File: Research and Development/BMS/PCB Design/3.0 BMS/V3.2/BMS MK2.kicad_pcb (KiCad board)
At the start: 2 copper layers, 174.6 x 98.4 mm, 42 parts, among them J1 JST CONN OUT, J3 JST CONN IN, J4 B+, J7 B-, Q1 AO3400A, Q2 PN100, Q3 AO3407, Q4 AO3407, Q7 PN100, SW1 SW_DPDT_x2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

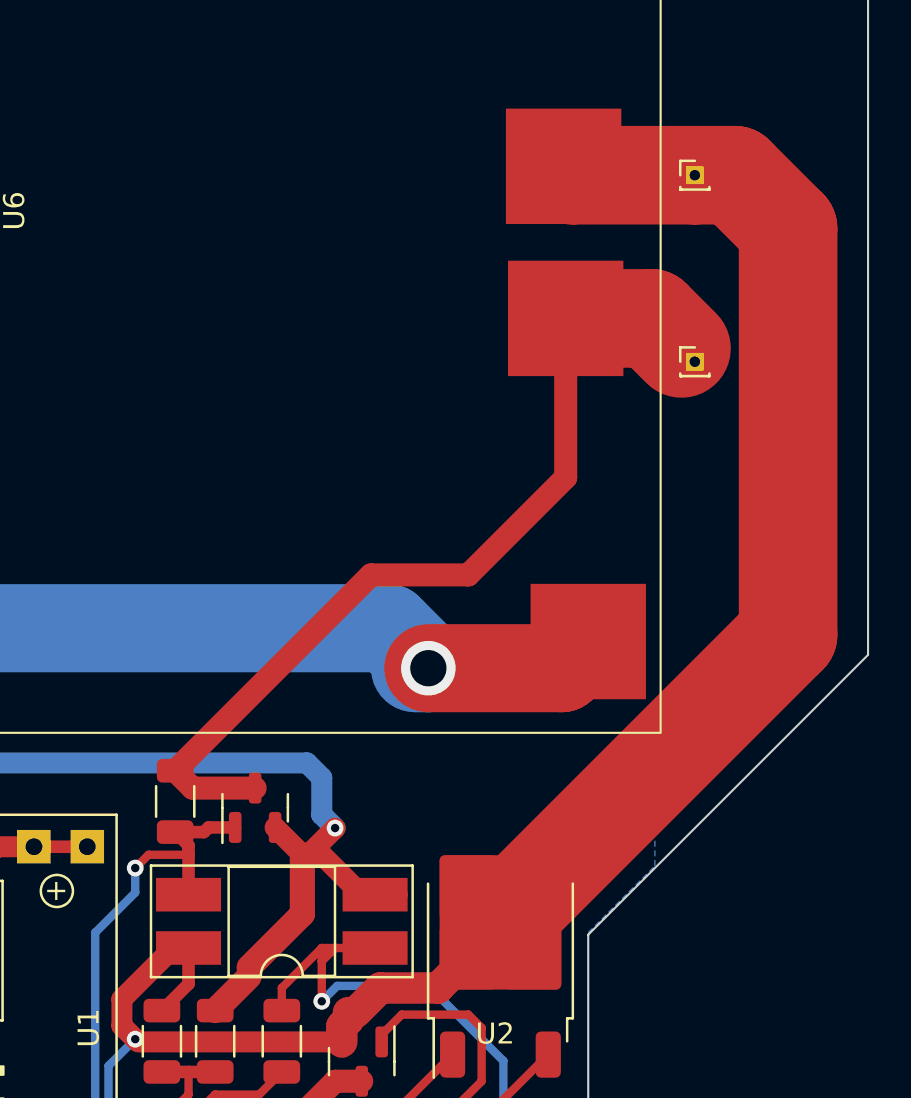
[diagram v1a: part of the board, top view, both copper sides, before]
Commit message: updated PCB and tidied up schematic BMS
Not final version. will revamp the charger in with 5 pins, 1 power for charging and powering load.
so charging section will be re implemented.

more 3d models added to board, bms etc
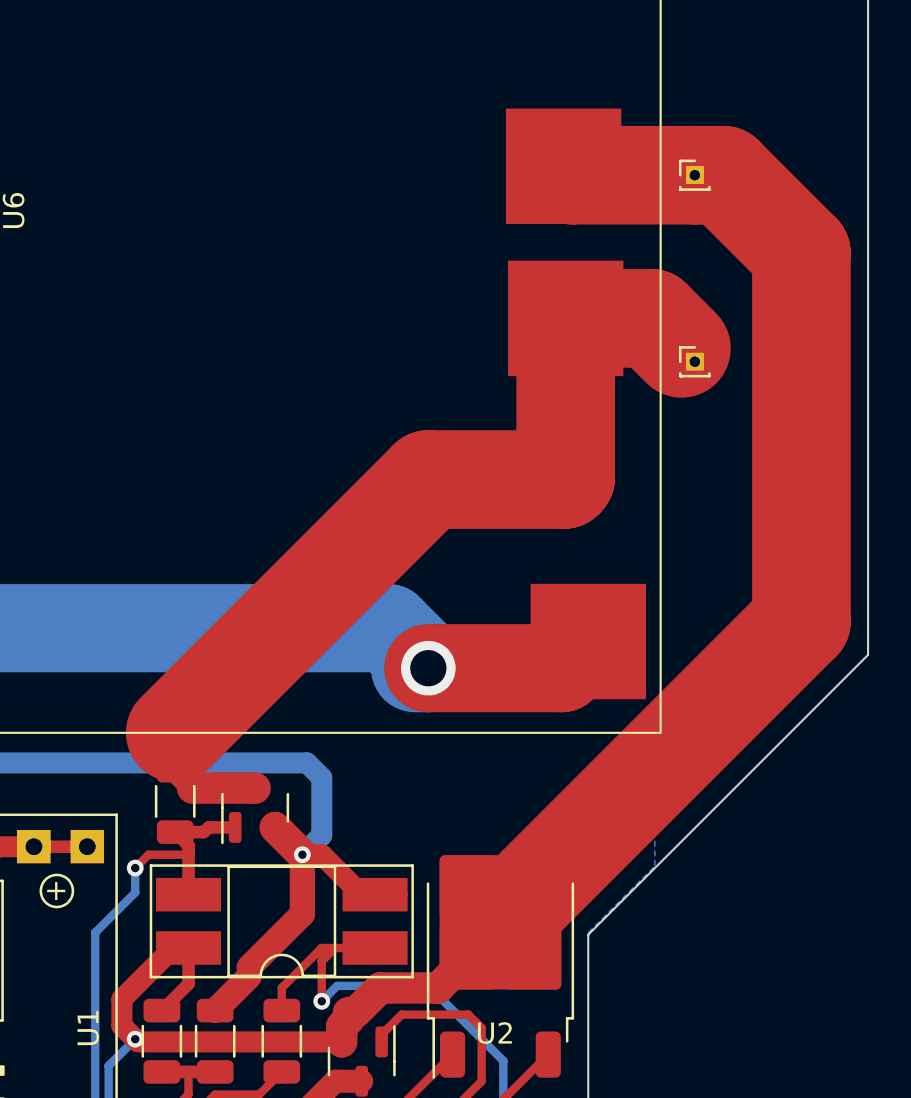
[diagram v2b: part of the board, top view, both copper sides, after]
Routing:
- net Batt -: track 42.5 -> 41.7 mm
- net GND: track 304.4 -> 303.7 mm
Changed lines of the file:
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@@
     (pad "7" smd rect (at 39.825 -3.9 90) (size 5.5 5.5) (layers "F.Cu" "F.Paste" "F.Mask")
       (net 24 "Net-(B4-B1-)") (pinfunction "16.8V") (pintype "input"))
+    (model "C:/Users/acste/Downloads/bms-4s-40a-60a-1.snapshot.2/BMS 4S 40A.STEP"
+      (offset (xyz 45.5 0 0))
+      (scale (xyz 1 1 1))
+      (rotate (xyz 0 0 -90))
+    )
   )
   (footprint "Capacitor_SMD:C_1206_3216Metric" (layer "F.Cu")
@@
   (segment (start 197.32 134.21) (end 195.58 135.95) (width 0.4) (layer "F.Cu") (net 1))
   (segment (start 201.295 115.57) (end 201.295 114.3) (width 1) (layer "F.Cu") (net 1))
+  (segment (start 229.97 75.03) (end 228.6 75.03) (width 4.7) (layer "F.Cu") (net 1))
   (segment (start 203.735 111.86) (end 204.47 111.86) (width 0.4) (layer "F.Cu") (net 1))
   (segment (start 201.295 114.3) (end 203.735 111.86) (width 1) (layer "F.Cu") (net 1))
   (segment (start 212.437501 114.935) (end 213.607501 113.765) (width 1.5) (layer "F.Cu") (net 1))
   (segment (start 204.47 111.86) (end 204.47 113.5725) (width 0.6) (layer "F.Cu") (net 1))
-  (segment (start 233.045 77.57) (end 230.505 75.03) (width 4.7) (layer "F.Cu") (net 1))
-  (segment (start 233.045 96.93) (end 233.045 77.57) (width 4.7) (layer "F.Cu") (net 1))
+  (segment (start 219.335 110.64) (end 233.68 96.295) (width 4.7) (layer "F.Cu") (net 1))
   (segment (start 216.36 113.765) (end 217.81 112.315) (width 1.5) (layer "F.Cu") (net 1))
+  (segment (start 233.68 78.74) (end 229.97 75.03) (width 4.7) (layer "F.Cu") (net 1))
   (segment (start 211.775 116.335) (end 211.775 115.597501) (width 1.5) (layer "F.Cu") (net 1))
   (segment (start 211.775 115.597501) (end 212.09 115.282501) (width 1.5) (layer "F.Cu") (net 1))
   (segment (start 197.32 132.345) (end 197.32 134.21) (width 0.4) (layer "F.Cu") (net 1))
-  (segment (start 230.505 75.03) (end 228.6 75.03) (width 4.7) (layer "F.Cu") (net 1))
+  (segment (start 233.68 96.295) (end 233.68 78.74) (width 4.7) (layer "F.Cu") (net 1))
   (segment (start 201.93 116.205) (end 201.295 115.57) (width 1) (layer "F.Cu") (net 1))
   (segment (start 212.09 115.282501) (end 212.09 114.935) (width 1.5) (layer "F.Cu") (net 1))
@@
   (segment (start 202.06 116.335) (end 211.775 116.335) (width 1) (layer "F.Cu") (net 1))
   (segment (start 213.607501 113.765) (end 216.36 113.765) (width 1.5) (layer "F.Cu") (net 1))
-  (segment (start 219.335 110.64) (end 233.045 96.93) (width 4.7) (layer "F.Cu") (net 1))
   (segment (start 204.47 113.5725) (end 203.2 114.8425) (width 0.6) (layer "F.Cu") (net 1))
   (segment (start 201.93 116.205) (end 202.06 116.335) (width 0.4) (layer "F.Cu") (net 1))
@@
   (segment (start 200.66 119.48) (end 203.835 122.655) (width 0.4) (layer "B.Cu") (net 1))
   (segment (start 203.835 126.1475) (end 199.39 130.91) (width 0.4) (layer "B.Cu") (net 1))
-  (segment (start 222.445 89.44) (end 222.445 81.855) (width 1.1) (layer "F.Cu") (net 2))
+  (segment (start 222.35 89.535) (end 222.445 89.44) (width 4.7) (layer "F.Cu") (net 2))
   (segment (start 222.605 82.015) (end 222.445 81.855) (width 2.2) (layer "F.Cu") (net 2))
+  (segment (start 222.445 89.44) (end 222.445 81.855) (width 4.7) (layer "F.Cu") (net 2))
+  (segment (start 215.9 89.535) (end 222.35 89.535) (width 4.7) (layer "F.Cu") (net 2))
+  (segment (start 203.835 101.6) (end 215.9 89.535) (width 4.7) (layer "F.Cu") (net 2))
   (segment (start 222.445 81.855) (end 226.535 81.855) (width 4.7) (layer "F.Cu") (net 2))
   (segment (start 204.6625 104.24) (end 203.835 103.4125) (width 1.1) (layer "F.Cu") (net 2))
-  (segment (start 203.835 103.4125) (end 213.1675 94.08) (width 1.1) (layer "F.Cu") (net 2))
-  (segment (start 217.805 94.08) (end 222.445 89.44) (width 1.1) (layer "F.Cu") (net 2))
-  (segment (start 213.1675 94.08) (end 217.805 94.08) (width 1.1) (layer "F.Cu") (net 2))
   (segment (start 226.535 81.855) (end 227.965 83.285) (width 4.7) (layer "F.Cu") (net 2))
-  (segment (start 207.645 104.24) (end 204.6625 104.24) (width 1.1) (layer "F.Cu") (net 2))
+  (segment (start 207.645 104.24) (end 204.6625 104.24) (width 1.5) (layer "F.Cu") (net 2))
   (segment (start 211.455 118.21) (end 209.55 120.115) (width 1.1) (layer "F.Cu") (net 3))
   (segment (start 205.813502 120.115) (end 204.543502 121.385) (width 1.1) (layer "F.Cu") (net 3))
@@
   (segment (start 180.98 136.63) (end 180.345 135.995) (width 0.4) (layer "F.Cu") (net 29))
   (segment (start 169.545 112.495) (end 165.1 112.495) (width 0.4) (layer "F.Cu") (net 29))
-  (segment (start 209.895 107.415) (end 210.185 107.415) (width 1) (layer "F.Cu") (net 29))
   (segment (start 178.562 118.21) (end 186.182 125.83) (width 0.6) (layer "F.Cu") (net 29))
   (segment (start 203.2 135.355) (end 203.845 136) (width 1.2) (layer "F.Cu") (net 29))
@@
   (segment (start 134.62 122.02) (end 118.92 106.32) (width 0.4) (layer "F.Cu") (net 29))
   (segment (start 209.895 107.415) (end 210.82 107.415) (width 1) (layer "F.Cu") (net 29))
-  (segment (start 208.595 106.115) (end 209.895 107.415) (width 1) (layer "F.Cu") (net 29))
+  (segment (start 208.595 106.115) (end 209.895 107.415) (width 1.5) (layer "F.Cu") (net 29))
   (segment (start 180.345 135.995) (end 177.17 135.995) (width 0.4) (layer "F.Cu") (net 29))
   (segment (start 161.29 122.02) (end 134.62 122.02) (width 0.4) (layer "F.Cu") (net 29))
   (segment (start 200.66 138.53) (end 201.93 139.8) (width 0.4) (layer "F.Cu") (net 29))
-  (segment (start 210.185 107.415) (end 211.455 106.145) (width 1) (layer "F.Cu") (net 29))
   (segment (start 209.895 107.415) (end 209.895 110.245) (width 1.2) (layer "F.Cu") (net 29))
   (segment (start 177.17 140.725) (end 177.17 135.995) (width 0.4) (layer "F.Cu") (net 29))
@@
   (via (at 203.2 135.355) (size 0.8) (drill 0.4) (layers "F.Cu" "B.Cu") (net 29))
   (via (at 176.535 135.658) (size 0.8) (drill 0.4) (layers "F.Cu" "B.Cu") (net 29))
-  (via (at 211.455 106.145) (size 0.8) (drill 0.4) (layers "F.Cu" "B.Cu") (net 29))
+  (via (at 209.895 107.415) (size 0.8) (drill 0.4) (layers "F.Cu" "B.Cu") (net 29))
   (via (at 169.545 148.055) (size 0.8) (drill 0.4) (layers "F.Cu" "B.Cu") (net 29))
   (via (at 188.595 104.875) (size 0.8) (drill 0.4) (layers "F.Cu" "B.Cu") (net 29))
@@
   (via (at 190.5 144.245) (size 0.8) (drill 0.4) (layers "F.Cu" "B.Cu") (net 29))
   (via (at 170.815 134.085) (size 0.8) (drill 0.4) (layers "F.Cu" "B.Cu") (net 29))
-  (segment (start 210.82 105.51) (end 210.82 103.745) (width 1) (layer "B.Cu") (net 29))
   (segment (start 196.460393 147.174607) (end 200.66 142.975) (width 1.2) (layer "B.Cu") (net 29))
-  (segment (start 211.455 106.145) (end 210.82 105.51) (width 1) (layer "B.Cu") (net 29))
   (segment (start 182.245 106.78) (end 184.15 104.875) (width 0.6) (layer "B.Cu") (net 29))
   (segment (start 182.245 110.49) (end 182.245 106.78) (width 0.6) (layer "B.Cu") (net 29))
   (segment (start 187.99 148.085) (end 169.575 148.085) (width 0.6) (layer "B.Cu") (net 29))
   (segment (start 174.962 134.085) (end 170.815 134.085) (width 0.4) (layer "B.Cu") (net 29))
+  (segment (start 209.895 107.415) (end 210.82 106.49) (width 1) (layer "B.Cu") (net 29))
+  (segment (start 172.085 145.515) (end 172.085 135.355) (width 0.6) (layer "B.Cu") (net 29))
   (segment (start 210.115 103.04) (end 192.335 103.04) (width 1) (layer "B.Cu") (net 29))
-  (segment (start 172.085 145.515) (end 172.085 135.355) (width 0.6) (layer "B.Cu") (net 29))
+  (segment (start 190.5 104.875) (end 188.595 104.875) (width 1) (layer "B.Cu") (net 29))
   (segment (start 169.575 148.085) (end 169.545 148.055) (width 0.6) (layer "B.Cu") (net 29))
   (segment (start 190.47 148.085) (end 194.28 148.085) (width 1.2) (layer "B.Cu") (net 29))
-  (segment (start 190.5 104.875) (end 188.595 104.875) (width 1) (layer "B.Cu") (net 29))
   (segment (start 170.815 114.4) (end 170.815 118.21) (width 0.6) (layer "B.Cu") (net 29))
+  (segment (start 192.335 103.04) (end 190.5 104.875) (width 1) (layer "B.Cu") (net 29))
   (segment (start 200.66 138.039214) (end 203.2 135.499214) (width 1.2) (layer "B.Cu") (net 29))
-  (segment (start 210.82 103.745) (end 210.115 103.04) (width 1) (layer "B.Cu") (net 29))
   (segment (start 189.865 148.69) (end 188.595 148.69) (width 0.6) (layer "B.Cu") (net 29))
   (segment (start 176.535 135.658) (end 174.962 134.085) (width 0.4) (layer "B.Cu") (net 29))
   (segment (start 203.2 135.499214) (end 203.2 135.355) (width 1.2) (layer "B.Cu") (net 29))
+  (segment (start 210.82 103.745) (end 210.115 103.04) (width 1) (layer "B.Cu") (net 29))
   (segment (start 179.07 111.76) (end 180.975 111.76) (width 0.6) (layer "B.Cu") (net 29))
   (segment (start 169.545 148.055) (end 172.085 145.515) (width 0.6) (layer "B.Cu") (net 29))
@@
   (segment (start 172.085 135.355) (end 170.815 134.085) (width 0.6) (layer "B.Cu") (net 29))
   (segment (start 176.43 114.4) (end 179.07 111.76) (width 0.6) (layer "B.Cu") (net 29))
+  (segment (start 210.82 106.49) (end 210.82 103.745) (width 1) (layer "B.Cu") (net 29))
   (segment (start 200.66 142.975) (end 200.66 138.039214) (width 1.2) (layer "B.Cu") (net 29))
-  (segment (start 192.335 103.04) (end 190.5 104.875) (width 1) (layer "B.Cu") (net 29))
   (segment (start 190.5 148.055) (end 190.47 148.085) (width 0.4) (layer "B.Cu") (net 29))
   (segment (start 188.595 148.69) (end 187.99 148.085) (width 0.6) (layer "B.Cu") (net 29))

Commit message: updated bms schem and pcb and added initial schem for charger
fixed charging switch logic for bms board, updated jst conns and now instead uses the supply v as the sw V+ to turn off the mosfet to then charge. should work considering it takes 100ns ~ to switch. added caps in schem but still havent calculated their values, nor are they on the pcb.

created the initial schematic from my notes for a charger that works in respect to the BMS board, is in the same cad file but different sheet to bms and is a seperate pcb.

still need to finalise the caps and also determine pcb via diameters with what i have available and the size requirements. will follow the suggestion for via size from kicad forum
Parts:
- removed U8: L78L05_SOT89, Package_TO_SOT_SMD:SOT-89-3
- added A1: Arduino_Nano_v3.x, Module:Arduino_Nano, F.Cu at (77.3, 128.1)
- added J2: Charger out, Connector_JST:JST_GH_SM04B-GHS-TB_1x04-1MP_P1.25mm_Horizontal, F.Cu at (47.0, 82.4)
- added J5: CHG IN, Connector_JST:JST_GH_SM04B-GHS-TB_1x04-1MP_P1.25mm_Horizontal, F.Cu at (250.8, 149.0)
- added Q5: PN100, Package_TO_SOT_SMD:SOT-23, F.Cu at (57.6, 115.9)
- added R13: 10K, Resistor_SMD:R_1206_3216Metric, F.Cu at (57.3, 119.7)
- added R5: 1.8K, Resistor_SMD:R_1206_3216Metric, F.Cu at (253.4, 136.9)
- added U10: ~, Package_TO_SOT_SMD:TO-252-2, F.Cu at (53.1, 128.7)
- added U9: L78L05_SOT89, Package_TO_SOT_SMD:SOT-89-3, F.Cu at (51.1, 121.7)
- J1: value JST CONN OUT -> Conn_01x04_Socket
- J3: value JST CONN IN -> PWR IN; footprint Connector_JST:JST_GH_SM04B-GHS-TB_1x04-1MP_P1.25mm_Horizontal -> Connector_JST:JST_GH_SM02B-GHS-TB_1x02-1MP_P1.25mm_Horizontal
- R3: value 430R -> 3k3
- moved J3 161.5 mm to (54.4, 83.6)
- moved R3 149.9 mm to (57.3, 123.0), turned to 180 degrees
- moved REF** 68.0 mm to (273.8, 158.2)
- moved U2 45.5 mm to (262.8, 125.5)
- moved J1 44.1 mm to (238.0, 158.4)
- moved C1 43.9 mm to (214.2, 148.6)
- moved Q3 43.9 mm to (228.7, 159.2)
- moved R2 43.9 mm to (209.3, 147.0)
- moved R7 43.9 mm to (224.9, 158.9)
- moved R8 43.9 mm to (221.1, 148.7)
- moved R9 43.9 mm to (221.1, 158.9)
- moved U3 43.9 mm to (214.3, 151.6)
- moved Q2 43.9 mm to (224.9, 153.5)
- moved Q4 43.9 mm to (254.8, 130.0)
- moved Q7 43.9 mm to (221.1, 153.5)
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- renumbered J4 to TP1, J7 to TP2
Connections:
- net Batt + renamed +BATT
- net Batt - renamed -BATT
- net Reg Batt 9v renamed +9V
- J1 pad 3: unconnected-(J1-Pin_3-Pad3) -> Battery Vref
- J3 pad 1: Chgr operating 12V+ -> GND1
- J3 pad 2: Chgr sgl 15V+ -> VD
- Q3 pad 1: DCG SW VCC -> CGE SW V+
- Q4 pad 1: Chgr sgl 15V+ -> Net-(Q4-G)
- Q4 pad 3: Chgr operating 12V+ -> +VDC
- R3 pad 1: charger GND bypass -> Net-(Q5-B)
- R3 pad 2: Net-(R12-Pad2) -> Net-(A1-D13)
- R7 pad 2: DCG SW VCC -> CGE SW V+
- R9 pad 1: CGE SW VCC -> CGE SW V+
- U1 pad 1: Chgr operating 12V+ -> +VDC
- U2 pad 1: Charge supplied VCC -> +VDC
- U2 pad 3: CGE SW VCC -> CGE SW V+
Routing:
- net -BATT: track 41.7 -> 118.9 mm, vias 0 -> 2
- net +VDC: track 0.00 -> 75.6 mm
- net CGE SW V+: track 0.00 -> 72.0 mm, vias 0 -> 2
- net CGE SW VCC: track 65.5 -> 0.00 mm, vias 2 -> 0
- net Chgr sgl 15V+: track 49.3 -> 0.00 mm
- net Battery Vref: track 37.5 -> 86.4 mm
- net Chgr operating 12V+: track 37.4 -> 0.00 mm
- net Net-(R12-Pad2): track 39.7 -> 6.31 mm, vias 2 -> 0
- net Charge supplied VCC: track 28.0 -> 0.00 mm
- net GND: track 303.7 -> 287.5 mm, vias 10 -> 9
- net Net-(B1-B1-): track 203.4 -> 211.6 mm
- net Net-(Q4-G): track 0.00 -> 7.74 mm
- net OUT 9V+ : track 15.4 -> 10.2 mm
- net DCG SW VCC: track 2.95 -> 0.00 mm
- net charger GND bypass: track 2.37 -> 0.00 mm
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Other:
- board size 174.6 x 98.4 mm -> 246.6 x 98.4 mm

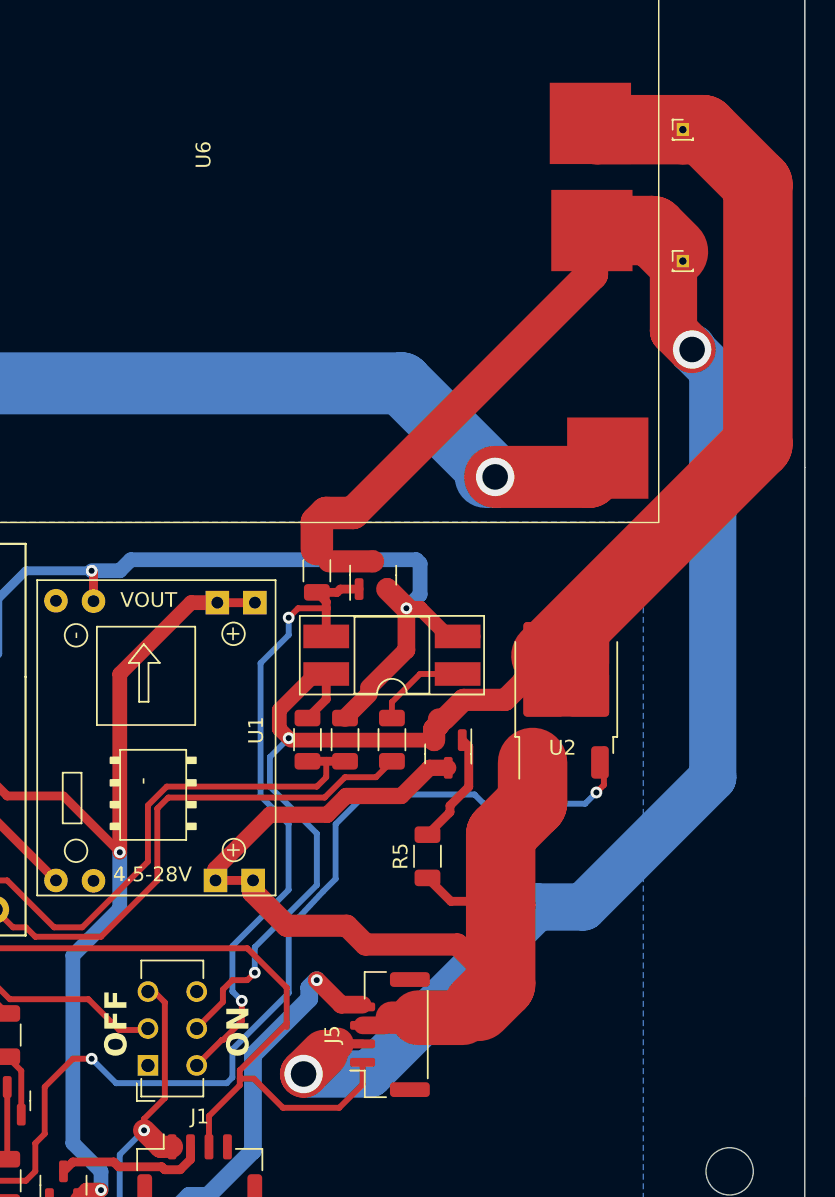
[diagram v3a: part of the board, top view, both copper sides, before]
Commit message: updated trace constraints and updated existing traces on board to suit their current
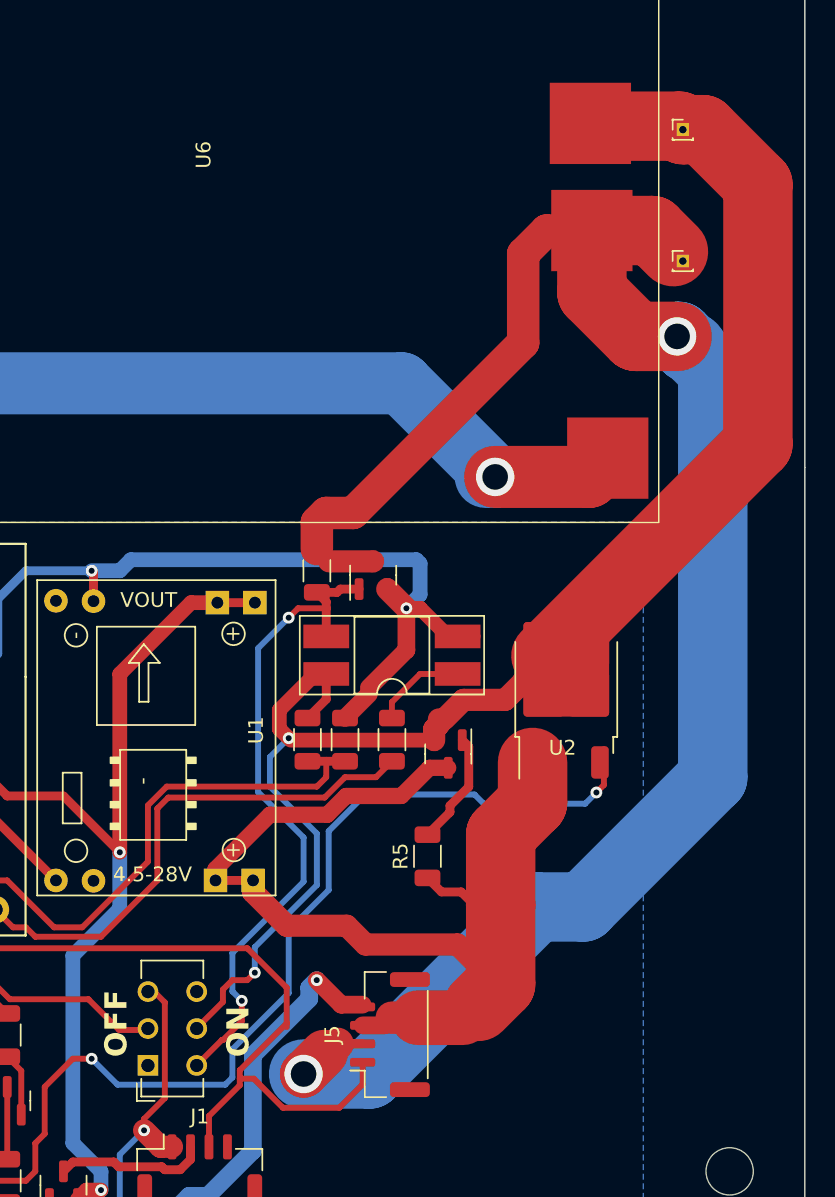
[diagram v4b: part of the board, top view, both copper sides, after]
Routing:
- net -BATT: track 118.9 -> 127.3 mm
- net Net-(Q1-G): track 44.2 -> 45.2 mm
